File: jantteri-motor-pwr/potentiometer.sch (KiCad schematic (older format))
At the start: 3 parts, among them J4 POT

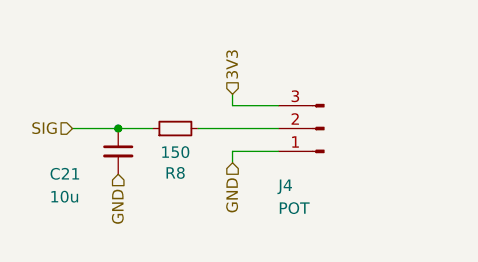
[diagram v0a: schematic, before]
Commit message: Tuubijantteri design Ordered
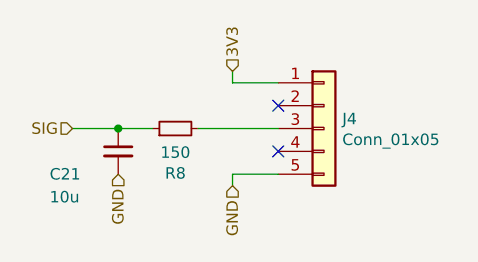
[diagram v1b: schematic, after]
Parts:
- removed J4: POT, Connector_JST:JST_ZH_B3B-ZR_1x03_P1.50mm_Vertical, symbol Connector:Conn_01x03_Male
- added J4: Conn_01x05, Connector_PinSocket_2.54mm:PinSocket_1x05_P2.54mm_Vertical, symbol Connector_Generic:Conn_01x05
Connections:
- net 3V3: now also J4.1 (Pin_1)
- net GND: now also J4.5 (Pin_5)
- net at R8.2: now also J4.3 (Pin_3)
- no-connect marks 0 -> 2
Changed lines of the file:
@@
 $Descr A4 11693 8268
 encoding utf-8
-Sheet 10 10
+Sheet 6 12
 Title ""
 Date ""
@@
 Comment4 ""
 $EndDescr
-$Comp
-L Connector:Conn_01x03_Male J4
-U 1 1 60271D3A
-P 7150 3100
-F 0 "J4" H 7350 3350 50  0000 R CNN
-F 1 "POT" H 7350 3450 50  0000 R CNN
-F 2 "Connector_JST:JST_ZH_B3B-ZR_1x03_P1.50mm_Vertical" H 7150 3100 50  0001 C CNN
-F 3 "~" H 7150 3100 50  0001 C CNN
-	1    7150 3100
-	-1   0    0    1
-$EndComp
 $Comp
 L Device:R_Small R8
@@
 	6250 3100 6400 3100
 Wire Wire Line
-	6750 2950 6750 3000
+	6750 2850 6750 2900
 Wire Wire Line
-	6750 3000 6950 3000
+	6750 2900 6950 2900
 Wire Wire Line
-	6950 3200 6750 3200
+	6950 3300 6750 3300
 Wire Wire Line
-	6750 3200 6750 3250
+	6750 3300 6750 3350
 Wire Wire Line
 	6600 3100 6950 3100
 Text HLabel 6050 3100 0    50   Input ~ 0
 SIG
-Text HLabel 6750 2950 1    50   Input ~ 0
+Text HLabel 6750 2850 1    50   Input ~ 0
 3V3
 Text HLabel 6250 3300 3    50   Input ~ 0
 GND
-Text HLabel 6750 3250 3    50   Input ~ 0
+Text HLabel 6750 3350 3    50   Input ~ 0
 GND
+$Comp
+L Connector_Generic:Conn_01x05 J4
+U 1 1 628FB63B
+P 7150 3100
+F 0 "J4" H 7230 3142 50  0000 L CNN
+F 1 "Conn_01x05" H 7230 3051 50  0000 L CNN
+F 2 "Connector_PinSocket_2.54mm:PinSocket_1x05_P2.54mm_Vertical" H 7150 3100 50  0001 C CNN
+F 3 "~" H 7150 3100 50  0001 C CNN
+	1    7150 3100
+	1    0    0    -1
+$EndComp
+NoConn ~ 6950 3000
+NoConn ~ 6950 3200
 $EndSCHEMATC
